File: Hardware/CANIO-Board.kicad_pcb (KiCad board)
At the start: 4 copper layers, 0 parts

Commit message: Finished the board
- Board layout and routing is finished. Need to fix ~30 ERC errors and
  add thorough notes throughout, but otherwise that's it.
- Once ERC errors are resolved, will post BOM and Gerbers as a release.
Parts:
- added BUCK1: AP63203QWU-7, Package_TO_SOT_SMD:TSOT-23-6, F.Cu at (193.8, 110.5)
- added BUCK2: AP63205QWU-7, Package_TO_SOT_SMD:TSOT-23-6, F.Cu at (193.7, 96.3)
- added C1: 1u, Capacitor_SMD:C_0603_1608Metric_Pad1.08x0.95mm_HandSolder, F.Cu at (130.0, 147.0)
- added C10: 100n, Capacitor_SMD:C_0603_1608Metric_Pad1.08x0.95mm_HandSolder, F.Cu at (161.1, 140.6)
- added C11: 10u, Capacitor_SMD:C_0603_1608Metric_Pad1.08x0.95mm_HandSolder, F.Cu at (144.7, 145.5)
- added C12: 100n, Capacitor_SMD:C_0603_1608Metric_Pad1.08x0.95mm_HandSolder, F.Cu at (144.7, 147.5)
- added C13: 22n, Capacitor_SMD:C_0603_1608Metric_Pad1.08x0.95mm_HandSolder, F.Cu at (161.1, 136.9)
- added C14: 22n, Capacitor_SMD:C_0603_1608Metric_Pad1.08x0.95mm_HandSolder, F.Cu at (159.6, 135.2)
- added C15: 100n, Capacitor_SMD:C_0603_1608Metric_Pad1.08x0.95mm_HandSolder, F.Cu at (197.8, 110.5)
- added C16: 22u, Capacitor_SMD:CP_Elec_4x4.5, F.Cu at (184.5, 116.0)
- added C17: 22u, Capacitor_SMD:CP_Elec_4x4.5, F.Cu at (184.5, 110.1)
- added C18: 10u, Capacitor_SMD:C_0603_1608Metric_Pad1.08x0.95mm_HandSolder, F.Cu at (189.8, 110.5)
- added C19: 100n, Capacitor_SMD:C_0603_1608Metric_Pad1.08x0.95mm_HandSolder, F.Cu at (197.7, 96.3)
- added C2: 1u, Capacitor_SMD:C_0603_1608Metric_Pad1.08x0.95mm_HandSolder, F.Cu at (142.2, 147.0)
- added C20: 22u, Capacitor_SMD:CP_Elec_4x4.5, F.Cu at (184.6, 101.6)
- added C21: 22u, Capacitor_SMD:CP_Elec_4x4.5, F.Cu at (184.6, 95.7)
- added C22: 10u, Capacitor_SMD:C_0603_1608Metric_Pad1.08x0.95mm_HandSolder, F.Cu at (189.7, 96.3)
- added C23: 10u, Capacitor_SMD:C_0603_1608Metric_Pad1.08x0.95mm_HandSolder, B.Cu at (104.6, 102.3)
- added C24: 10u, Capacitor_SMD:C_0603_1608Metric_Pad1.08x0.95mm_HandSolder, B.Cu at (113.8, 105.7)
- added C25: 4.7u, Capacitor_SMD:CP_Elec_4x4.5, F.Cu at (104.2, 101.3)
- added C26: 10n, Capacitor_SMD:C_0603_1608Metric_Pad1.08x0.95mm_HandSolder, B.Cu at (109.0, 116.0)
- added C27: 1u, Capacitor_SMD:C_0603_1608Metric_Pad1.08x0.95mm_HandSolder, F.Cu at (140.2, 134.0)
- added C3: 1u, Capacitor_SMD:C_0603_1608Metric_Pad1.08x0.95mm_HandSolder, F.Cu at (170.0, 147.0)
- added C4: 1u, Capacitor_SMD:C_0603_1608Metric_Pad1.08x0.95mm_HandSolder, F.Cu at (182.2, 147.0)
- added C5: 1u, Capacitor_SMD:C_0603_1608Metric_Pad1.08x0.95mm_HandSolder, F.Cu at (130.0, 159.0)
- added C6: 1u, Capacitor_SMD:C_0603_1608Metric_Pad1.08x0.95mm_HandSolder, F.Cu at (142.1, 157.1)
- added C7: 1u, Capacitor_SMD:C_0603_1608Metric_Pad1.08x0.95mm_HandSolder, F.Cu at (170.0, 159.0)
- added C8: 1u, Capacitor_SMD:C_0603_1608Metric_Pad1.08x0.95mm_HandSolder, F.Cu at (182.2, 159.0)
- added C9: 10u, Capacitor_SMD:C_0603_1608Metric_Pad1.08x0.95mm_HandSolder, F.Cu at (161.1, 138.6)
- added CAN1: ISO1042, Package_SO:SOIC-16W_7.5x10.3mm_P1.27mm, F.Cu at (107.8, 111.6)
- added DCDC1: NME1, footprints:NME1S, F.Cu at (112.5, 95.6)
- added DFB1: D_Small, Diode_THT:D_DO-35_SOD27_P7.62mm_Horizontal, F.Cu at (125.8, 109.5)
- added DFB2: D_Small, Diode_THT:D_DO-35_SOD27_P7.62mm_Horizontal, F.Cu at (133.4, 112.0)
- added DFB3: D_Small, Diode_THT:D_DO-35_SOD27_P7.62mm_Horizontal, F.Cu at (141.5, 109.5)
- added DFB4: D_Small, Diode_THT:D_DO-35_SOD27_P7.62mm_Horizontal, F.Cu at (149.2, 112.0)
- added DFB5: D_Small, Diode_THT:D_DO-35_SOD27_P7.62mm_Horizontal, F.Cu at (157.2, 109.5)
- added DFB6: D_Small, Diode_THT:D_DO-35_SOD27_P7.62mm_Horizontal, F.Cu at (165.0, 112.0)
- added DFB7: D_Small, Diode_THT:D_DO-35_SOD27_P7.62mm_Horizontal, F.Cu at (172.9, 109.5)
- added DFB8: D_Small, Diode_THT:D_DO-35_SOD27_P7.62mm_Horizontal, F.Cu at (179.9, 112.0)
- added DIP1: SW_DIP_x03, Button_Switch_THT:SW_DIP_SPSTx03_Slide_9.78x9.8mm_W7.62mm_P2.54mm, F.Cu at (113.5, 147.3)
- added DT1: Conn_01x02, footprints:TE_DTF13-2P, F.Cu at (186.3, 132.5)
- added DT2: Conn_01x03, footprints:TE_DTF13-3P, F.Cu at (112.2, 131.8)
- added FILTER1: ECMF02-2AMX6, footprints:ECMF02-2AMX6_QFN-6L, F.Cu at (105.3, 119.0)
- added FILTER2: ECMF02-2AMX6, footprints:ECMF02-2AMX6_QFN-6L, F.Cu at (150.0, 155.0)
- added H1: GND, MountingHole:MountingHole_3.5mm_Pad_Via, F.Cu at (104.2, 90.0)
- added H2: GND, MountingHole:MountingHole_3.5mm_Pad_Via, F.Cu at (195.8, 90.0)
- added H3: GND, MountingHole:MountingHole_3.5mm_Pad_Via, F.Cu at (195.8, 160.8)
- added H4: GND, MountingHole:MountingHole_3.5mm_Pad_Via, F.Cu at (104.2, 160.8)
- added J1: Conn_01x03, Connector_PinHeader_2.54mm:PinHeader_1x03_P2.54mm_Vertical, F.Cu at (119.2, 132.2)
- added J2: Conn_01x07, Connector_PinHeader_2.54mm:PinHeader_1x07_P2.54mm_Vertical, F.Cu at (185.4, 146.5)
- added L1: 4.7u, Inductor_THT:L_Axial_L7.0mm_D3.3mm_P5.08mm_Vertical_Fastron_MICC, F.Cu at (195.8, 115.5)
- added L2: 4.7u, Inductor_THT:L_Axial_L7.0mm_D3.3mm_P5.08mm_Vertical_Fastron_MICC, F.Cu at (195.7, 101.3)
- added L3: 47u, Inductor_THT:L_Axial_L7.0mm_D3.3mm_P5.08mm_Vertical_Fastron_MICC, F.Cu at (107.0, 96.7)
- added LDO1: SPX5205-ADJ, Package_TO_SOT_SMD:SOT-23-5_HandSoldering, B.Cu at (109.9, 105.7)
- added LED1: LED_Small, LED_SMD:LED_1206_3216Metric_Pad1.42x1.75mm_HandSolder, F.Cu at (155.5, 152.3)
- added LED2: LED_Small, LED_SMD:LED_1206_3216Metric_Pad1.42x1.75mm_HandSolder, F.Cu at (152.9, 152.3)
- added LED3: LED_Small, LED_SMD:LED_1206_3216Metric_Pad1.42x1.75mm_HandSolder, F.Cu at (179.2, 123.0)
- added LED4: LED_Small, LED_SMD:LED_1206_3216Metric_Pad1.42x1.75mm_HandSolder, F.Cu at (176.7, 123.0)
- added LOAD1: TBD62783AFWG, Package_SO:SOP-18_7x12.5mm_P1.27mm, F.Cu at (169.1, 119.5)
- added MCU1: STM32G0B1KETxN, Package_QFP:LQFP-32_7x7mm_P0.8mm, F.Cu at (150.0, 140.0)
- added R1: 10k, Resistor_SMD:R_0603_1608Metric_Pad0.98x0.95mm_HandSolder, F.Cu at (117.8, 143.0)
- added R10: 1k, Resistor_SMD:R_0603_1608Metric_Pad0.98x0.95mm_HandSolder, F.Cu at (152.9, 147.8)
- added R11: 1k, Resistor_SMD:R_0603_1608Metric_Pad0.98x0.95mm_HandSolder, F.Cu at (179.2, 118.0)
- added R12: 1k, Resistor_SMD:R_0603_1608Metric_Pad0.98x0.95mm_HandSolder, F.Cu at (176.7, 118.0)
- added R13: 17k, Resistor_SMD:R_0603_1608Metric_Pad0.98x0.95mm_HandSolder, B.Cu at (105.6, 105.7)
- added R14: 10k, Resistor_SMD:R_0603_1608Metric_Pad0.98x0.95mm_HandSolder, B.Cu at (103.6, 105.7)
- added R15: 60, Resistor_SMD:R_0603_1608Metric_Pad0.98x0.95mm_HandSolder, B.Cu at (109.0, 114.0)
- added R16: 60, Resistor_SMD:R_0603_1608Metric_Pad0.98x0.95mm_HandSolder, B.Cu at (109.0, 112.0)
- added R17: 5.1k, Resistor_SMD:R_0603_1608Metric_Pad0.98x0.95mm_HandSolder, F.Cu at (142.5, 161.2)
- added R18: 5.1k, Resistor_SMD:R_0603_1608Metric_Pad0.98x0.95mm_HandSolder, F.Cu at (157.5, 161.2)
- added R19: 10k, Resistor_SMD:R_0603_1608Metric_Pad0.98x0.95mm_HandSolder, F.Cu at (138.2, 134.0)
- added R2: 10k, Resistor_SMD:R_0603_1608Metric_Pad0.98x0.95mm_HandSolder, F.Cu at (130.0, 143.0)
- added R3: 10k, Resistor_SMD:R_0603_1608Metric_Pad0.98x0.95mm_HandSolder, F.Cu at (157.8, 143.0)
- added R4: 10k, Resistor_SMD:R_0603_1608Metric_Pad0.98x0.95mm_HandSolder, F.Cu at (170.0, 143.0)
- added R5: 10k, Resistor_SMD:R_0603_1608Metric_Pad0.98x0.95mm_HandSolder, F.Cu at (117.8, 155.0)
- added R6: 10k, Resistor_SMD:R_0603_1608Metric_Pad0.98x0.95mm_HandSolder, F.Cu at (130.0, 155.0)
- added R7: 10k, Resistor_SMD:R_0603_1608Metric_Pad0.98x0.95mm_HandSolder, F.Cu at (157.8, 155.0)
- added R8: 10k, Resistor_SMD:R_0603_1608Metric_Pad0.98x0.95mm_HandSolder, F.Cu at (170.0, 155.0)
- added R9: 1k, Resistor_SMD:R_0603_1608Metric_Pad0.98x0.95mm_HandSolder, F.Cu at (155.5, 147.8)
- added RELAY1: ALDP112W, footprints:RELAY_ALDP112W, F.Cu at (121.9, 95.8)
- added RELAY2: ALDP112W, footprints:RELAY_ALDP112W, F.Cu at (129.8, 95.8)
- added RELAY3: ALDP112W, footprints:RELAY_ALDP112W, F.Cu at (137.6, 95.8)
- added RELAY4: ALDP112W, footprints:RELAY_ALDP112W, F.Cu at (145.4, 95.8)
- added RELAY5: ALDP112W, footprints:RELAY_ALDP112W, F.Cu at (153.2, 95.8)
- added RELAY6: ALDP112W, footprints:RELAY_ALDP112W, F.Cu at (161.0, 95.8)
- added RELAY7: ALDP112W, footprints:RELAY_ALDP112W, F.Cu at (168.9, 95.8)
- added RELAY8: ALDP112W, footprints:RELAY_ALDP112W, F.Cu at (176.7, 95.8)
- added SB1: SolderJumper_2_Open, Jumper:SolderJumper-2_P1.3mm_Open_TrianglePad1.0x1.5mm, F.Cu at (122.0, 117.0)
- added SB10: SolderJumper_2_Open, Jumper:SolderJumper-2_P1.3mm_Open_TrianglePad1.0x1.5mm, F.Cu at (127.0, 120.0)
- added SB11: SolderJumper_2_Open, Jumper:SolderJumper-2_P1.3mm_Open_TrianglePad1.0x1.5mm, F.Cu at (131.9, 120.0)
- added SB12: SolderJumper_2_Open, Jumper:SolderJumper-2_P1.3mm_Open_TrianglePad1.0x1.5mm, F.Cu at (136.9, 120.0)
- added SB13: SolderJumper_2_Open, Jumper:SolderJumper-2_P1.3mm_Open_TrianglePad1.0x1.5mm, F.Cu at (141.9, 117.0)
- added SB14: SolderJumper_2_Open, Jumper:SolderJumper-2_P1.3mm_Open_TrianglePad1.0x1.5mm, F.Cu at (146.9, 117.0)
- added SB15: SolderJumper_2_Open, Jumper:SolderJumper-2_P1.3mm_Open_TrianglePad1.0x1.5mm, F.Cu at (151.9, 117.0)
- added SB16: SolderJumper_2_Open, Jumper:SolderJumper-2_P1.3mm_Open_TrianglePad1.0x1.5mm, F.Cu at (156.9, 117.0)
- added SB17: SolderJumper_2_Open, Jumper:SolderJumper-2_P1.3mm_Open_TrianglePad1.0x1.5mm, F.Cu at (141.9, 123.0)
- added SB18: SolderJumper_2_Open, Jumper:SolderJumper-2_P1.3mm_Open_TrianglePad1.0x1.5mm, F.Cu at (146.9, 123.0)
- added SB19: SolderJumper_2_Open, Jumper:SolderJumper-2_P1.3mm_Open_TrianglePad1.0x1.5mm, F.Cu at (151.9, 123.0)
- added SB2: SolderJumper_2_Open, Jumper:SolderJumper-2_P1.3mm_Open_TrianglePad1.0x1.5mm, F.Cu at (127.0, 117.0)
- added SB20: SolderJumper_2_Open, Jumper:SolderJumper-2_P1.3mm_Open_TrianglePad1.0x1.5mm, F.Cu at (156.9, 123.0)
- added SB21: SolderJumper_2_Open, Jumper:SolderJumper-2_P1.3mm_Open_TrianglePad1.0x1.5mm, F.Cu at (141.9, 120.0)
- added SB22: SolderJumper_2_Open, Jumper:SolderJumper-2_P1.3mm_Open_TrianglePad1.0x1.5mm, F.Cu at (146.9, 120.0)
- added SB23: SolderJumper_2_Open, Jumper:SolderJumper-2_P1.3mm_Open_TrianglePad1.0x1.5mm, F.Cu at (151.9, 120.0)
- added SB24: SolderJumper_2_Open, Jumper:SolderJumper-2_P1.3mm_Open_TrianglePad1.0x1.5mm, F.Cu at (156.9, 120.0)
- added SB3: SolderJumper_2_Open, Jumper:SolderJumper-2_P1.3mm_Open_TrianglePad1.0x1.5mm, F.Cu at (131.9, 117.0)
- added SB4: SolderJumper_2_Open, Jumper:SolderJumper-2_P1.3mm_Open_TrianglePad1.0x1.5mm, F.Cu at (136.9, 117.0)
- added SB5: SolderJumper_2_Open, Jumper:SolderJumper-2_P1.3mm_Open_TrianglePad1.0x1.5mm, F.Cu at (122.0, 123.0)
- added SB6: SolderJumper_2_Open, Jumper:SolderJumper-2_P1.3mm_Open_TrianglePad1.0x1.5mm, F.Cu at (127.0, 123.0)
- added SB7: SolderJumper_2_Open, Jumper:SolderJumper-2_P1.3mm_Open_TrianglePad1.0x1.5mm, F.Cu at (131.9, 123.0)
- added SB8: SolderJumper_2_Open, Jumper:SolderJumper-2_P1.3mm_Open_TrianglePad1.0x1.5mm, F.Cu at (136.9, 123.0)
- added SB9: SolderJumper_2_Open, Jumper:SolderJumper-2_P1.3mm_Open_TrianglePad1.0x1.5mm, F.Cu at (122.0, 120.0)
- added SCREW1: Conn_01x02, TerminalBlock:TerminalBlock_MaiXu_MX126-5.0-02P_1x02_P5.00mm, F.Cu at (171.2, 134.0)
- added SCREW2: Conn_01x03, TerminalBlock:TerminalBlock_MaiXu_MX126-5.0-03P_1x03_P5.00mm, F.Cu at (106.9, 136.3)
- added SW1: SW_Push, Button_Switch_SMD:SW_Push_1P1T_NO_CK_KSC7xxJ, F.Cu at (123.9, 145.0)
- added SW2: SW_Push, Button_Switch_SMD:SW_Push_1P1T_NO_CK_KSC7xxJ, F.Cu at (136.1, 145.0)
- added SW3: SW_Push, Button_Switch_SMD:SW_Push_1P1T_NO_CK_KSC7xxJ, F.Cu at (163.9, 145.0)
- added SW4: SW_Push, Button_Switch_SMD:SW_Push_1P1T_NO_CK_KSC7xxJ, F.Cu at (176.1, 145.0)
- added SW5: SW_Push, Button_Switch_SMD:SW_Push_1P1T_NO_CK_KSC7xxJ, F.Cu at (123.9, 157.0)
- added SW6: SW_Push, Button_Switch_SMD:SW_Push_1P1T_NO_CK_KSC7xxJ, F.Cu at (136.1, 157.0)
- added SW7: SW_Push, Button_Switch_SMD:SW_Push_1P1T_NO_CK_KSC7xxJ, F.Cu at (163.9, 157.0)
- added SW8: SW_Push, Button_Switch_SMD:SW_Push_1P1T_NO_CK_KSC7xxJ, F.Cu at (176.1, 157.0)
- added SW9: SW_Push, Button_Switch_SMD:SW_Push_1P1T_NO_CK_KSC7xxJ, F.Cu at (132.1, 134.1)
- added TC1: TC2030, Connector:Tag-Connect_TC2030-IDC-NL_2x03_P1.27mm_Vertical, F.Cu at (124.2, 135.1)
- added TVS1: D_TVS, Diode_SMD:D_SMA_Handsoldering, B.Cu at (181.6, 132.7)
- added TVS2: D_TVS_Dual_AAC, Package_TO_SOT_SMD:SOT-23, B.Cu at (115.8, 134.1)
- added TVS3: ESDS314DBVR, Package_TO_SOT_SMD:SOT-23-5, F.Cu at (123.1, 129.1)
- added TVS4: ESDS314DBVR, Package_TO_SOT_SMD:SOT-23-5, B.Cu at (190.8, 155.9)
- added TVS5: ESDS314DBVR, Package_TO_SOT_SMD:SOT-23-5, B.Cu at (190.8, 150.9)
- added USB1: USB_C_Receptacle_USB2.0_16P, footprints:SHOUHAN_TYPE-C_16PIN_2MD__073_, F.Cu at (150.0, 162.2)
- added WAGO1: 2601, TerminalBlock_WAGO:TerminalBlock_WAGO_2601-1102_1x02_P3.50mm_Horizontal, F.Cu at (109.5, 73.2)
- added WAGO2: 2601, TerminalBlock_WAGO:TerminalBlock_WAGO_2601-1102_1x02_P3.50mm_Horizontal, F.Cu at (121.6, 73.2)
- added WAGO3: 2601, TerminalBlock_WAGO:TerminalBlock_WAGO_2601-1102_1x02_P3.50mm_Horizontal, F.Cu at (133.7, 73.2)
- added WAGO4: 2601, TerminalBlock_WAGO:TerminalBlock_WAGO_2601-1102_1x02_P3.50mm_Horizontal, F.Cu at (145.8, 73.2)
- added WAGO5: 2601, TerminalBlock_WAGO:TerminalBlock_WAGO_2601-1102_1x02_P3.50mm_Horizontal, F.Cu at (157.9, 73.2)
- added WAGO6: 2601, TerminalBlock_WAGO:TerminalBlock_WAGO_2601-1102_1x02_P3.50mm_Horizontal, F.Cu at (170.0, 73.2)
- added WAGO7: 2601, TerminalBlock_WAGO:TerminalBlock_WAGO_2601-1102_1x02_P3.50mm_Horizontal, F.Cu at (182.1, 73.2)
- added WAGO8: 2601, TerminalBlock_WAGO:TerminalBlock_WAGO_2601-1102_1x02_P3.50mm_Horizontal, F.Cu at (194.2, 73.2)
- added Y1: Crystal, Crystal:Crystal_SMD_3215-2Pin_3.2x1.5mm, F.Cu at (157.0, 136.7)
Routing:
- net 3v3: track 0.00 -> 87.4 mm, vias 0 -> 17
- net /Load_Driver/Chan4: track 0.00 -> 85.6 mm, vias 0 -> 2
- net /Load_Driver/Chan7: track 0.00 -> 84.6 mm, vias 0 -> 2
- net /Load_Driver/Chan6: track 0.00 -> 84.3 mm, vias 0 -> 4
- net /Load_Driver/Chan5: track 0.00 -> 78.8 mm, vias 0 -> 2
- net /Connectors/DriverOutN7: track 0.00 -> 78.3 mm, vias 0 -> 1
- net /Load_Driver/Chan0: track 0.00 -> 72.4 mm, vias 0 -> 2
- net /Connectors/DriverOutN6: track 0.00 -> 70.8 mm, vias 0 -> 2
- net /Load_Driver/Chan3: track 0.00 -> 70.2 mm, vias 0 -> 2
- net /Connectors/DriverOutN5: track 0.00 -> 67.1 mm, vias 0 -> 2
- net /Connectors/DriverOutN4: track 0.00 -> 65.3 mm, vias 0 -> 2
- net /Connectors/DriverOutN2: track 0.00 -> 62.7 mm, vias 0 -> 2
- net /Connectors/DriverOutN1: track 0.00 -> 61.4 mm, vias 0 -> 2
- net /Connectors/DriverOutN3: track 0.00 -> 61.4 mm, vias 0 -> 2
- net /Load_Driver/Chan1: track 0.00 -> 60.7 mm, vias 0 -> 2
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- added copper zone on B.Cu, net +12V
- added copper zone on F.Cu, net 3v3
- added copper zone on In2.Cu, net 3v3
- added copper zone on F.Cu, net 5v0
- added copper zone on In2.Cu, net 5v0
- added copper zone on F.Cu, net CANGND
- added copper zone on In1.Cu, net CANGND
- added copper zone on B.Cu, net CANVDD
- added copper zone on F.Cu, net GND
- added copper zone on In1.Cu, net GND
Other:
- board outline added: 100 x 100 mm
- board text added: "- Board is centered at (150, 115), and is 100mm*100mm. - Corners have 3mm fillet. PTHs are 3.5mm (support M3 screws) - Bottom PTHs are 4.25mm away from both edges. Top ones are 4.25mm away from the left and right edges, and 25mm away from the top edge. These are all from edge of board to center of PTH. - MCU is 20mm below the center of the board, tilted 45 degrees for optimal routing. - Allocated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"
- board text added: "12V"
- board text added: "3v3"
- board text added: "5v0"
- board text added: "Design Notes"
- board text added: "GPIO6"
- board text added: "Info at njit-solar-car.github.io/canio"
- board text added: "Layer 1 - GND"
- board text added: "Layer 2 - GND"
- board text added: "Layer 4 - 12V"
- board text added: "Load Driver"
- board text added: "NO Copper Pour on In1 under CANH/L1!! Also, CANGND and CANVDD on top and bottom"
- board text added: "PB15"
- board text added: "PB6"
- board text added: "PB7"
- board text added: "PB8"
- board text added: "PB9 - GPIO0"
- board text added: "PD0"
- board text added: "PD1"
- board text added: "PD2"
- board text added: "PD3"
- board text added: "Reset"
- board text added: "SWD"
- board text added: "This entire area does not use 3v3 or 5v0. In2 can be used to route signals."

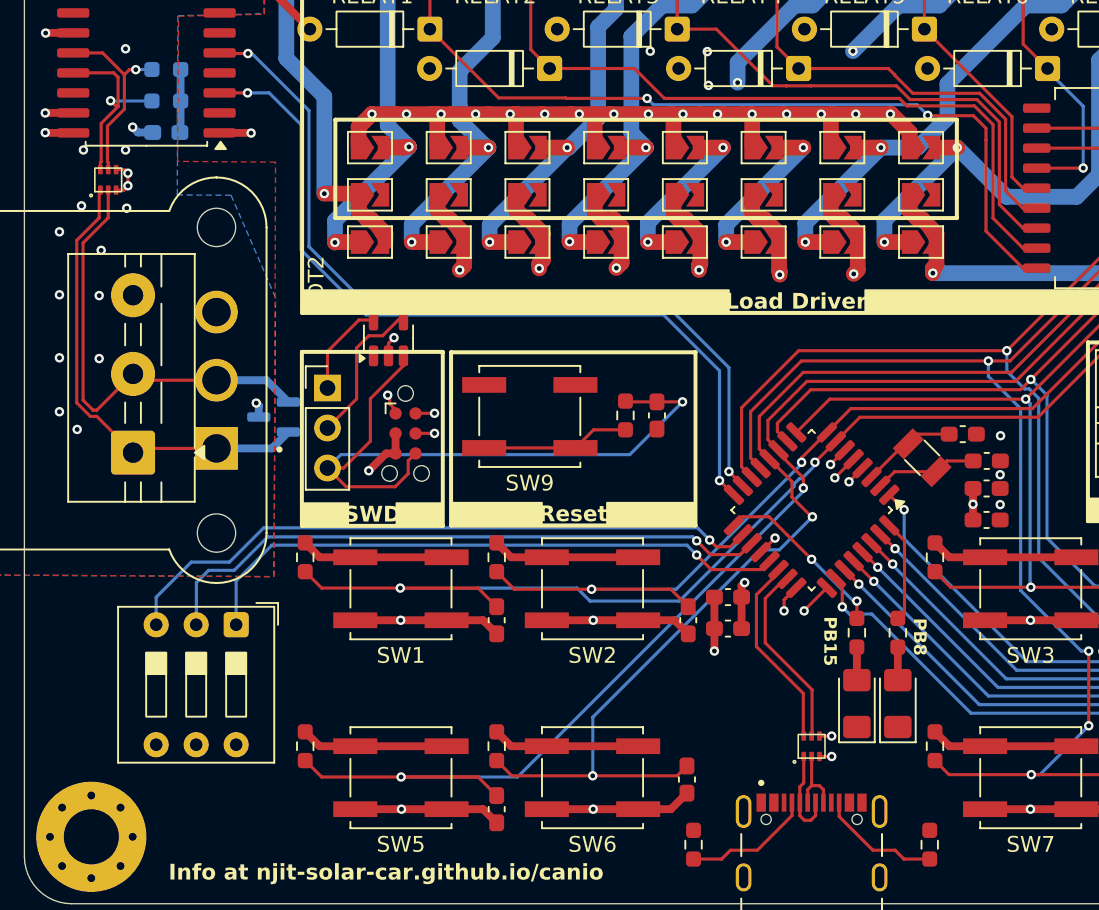
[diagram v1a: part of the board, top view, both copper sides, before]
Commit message: Fixed ERC errors
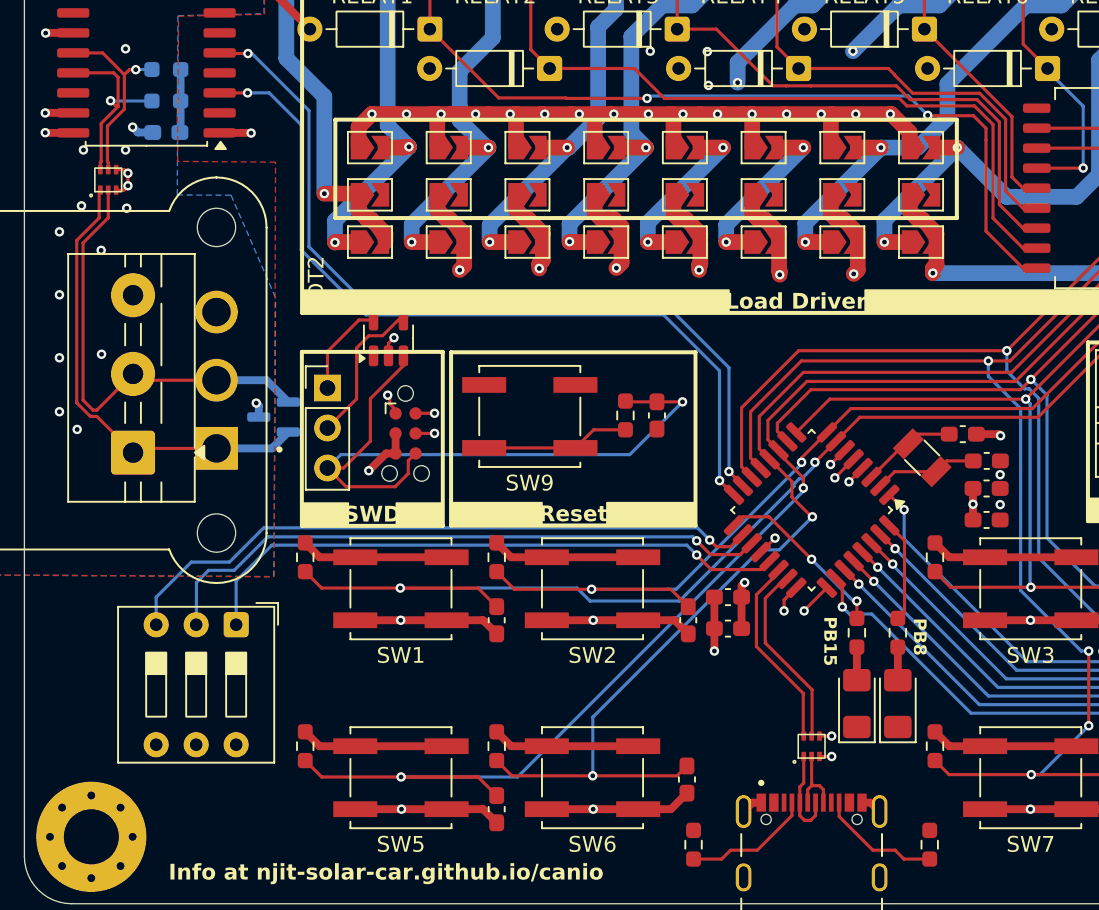
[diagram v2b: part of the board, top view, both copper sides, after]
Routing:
- net GND: track 32.6 -> 36.9 mm
- net CANGND: vias 26 -> 25

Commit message: final changes on pcb
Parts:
- added D1: D, Diode_SMD:D_SMC_Handsoldering, B.Cu at (174.8, 140.8)
- moved TVS1 3.89 mm to (180.9, 128.9), turned to -90 degrees
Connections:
- DT1 pad 1: +12V -> /Power/Raw12V
- SCREW1 pad 1: +12V -> /Power/Raw12V
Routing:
- added copper zone on B.Cu, net /Power/Raw12V
